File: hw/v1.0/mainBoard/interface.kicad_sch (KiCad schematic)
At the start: 30 parts, among them J1 MQ-7, J13 PM1003, J2 VEML7700, J3 SHT40, J5 ML8511, J7 BMP388, J8 PMS5003, Q16 2N7002, Q17 2N7002, Q3 AO3401A, Q4 2N7002, Q5 AO3401A, Q6 2N7002, Q7 AO3401A, Q8 2N7002

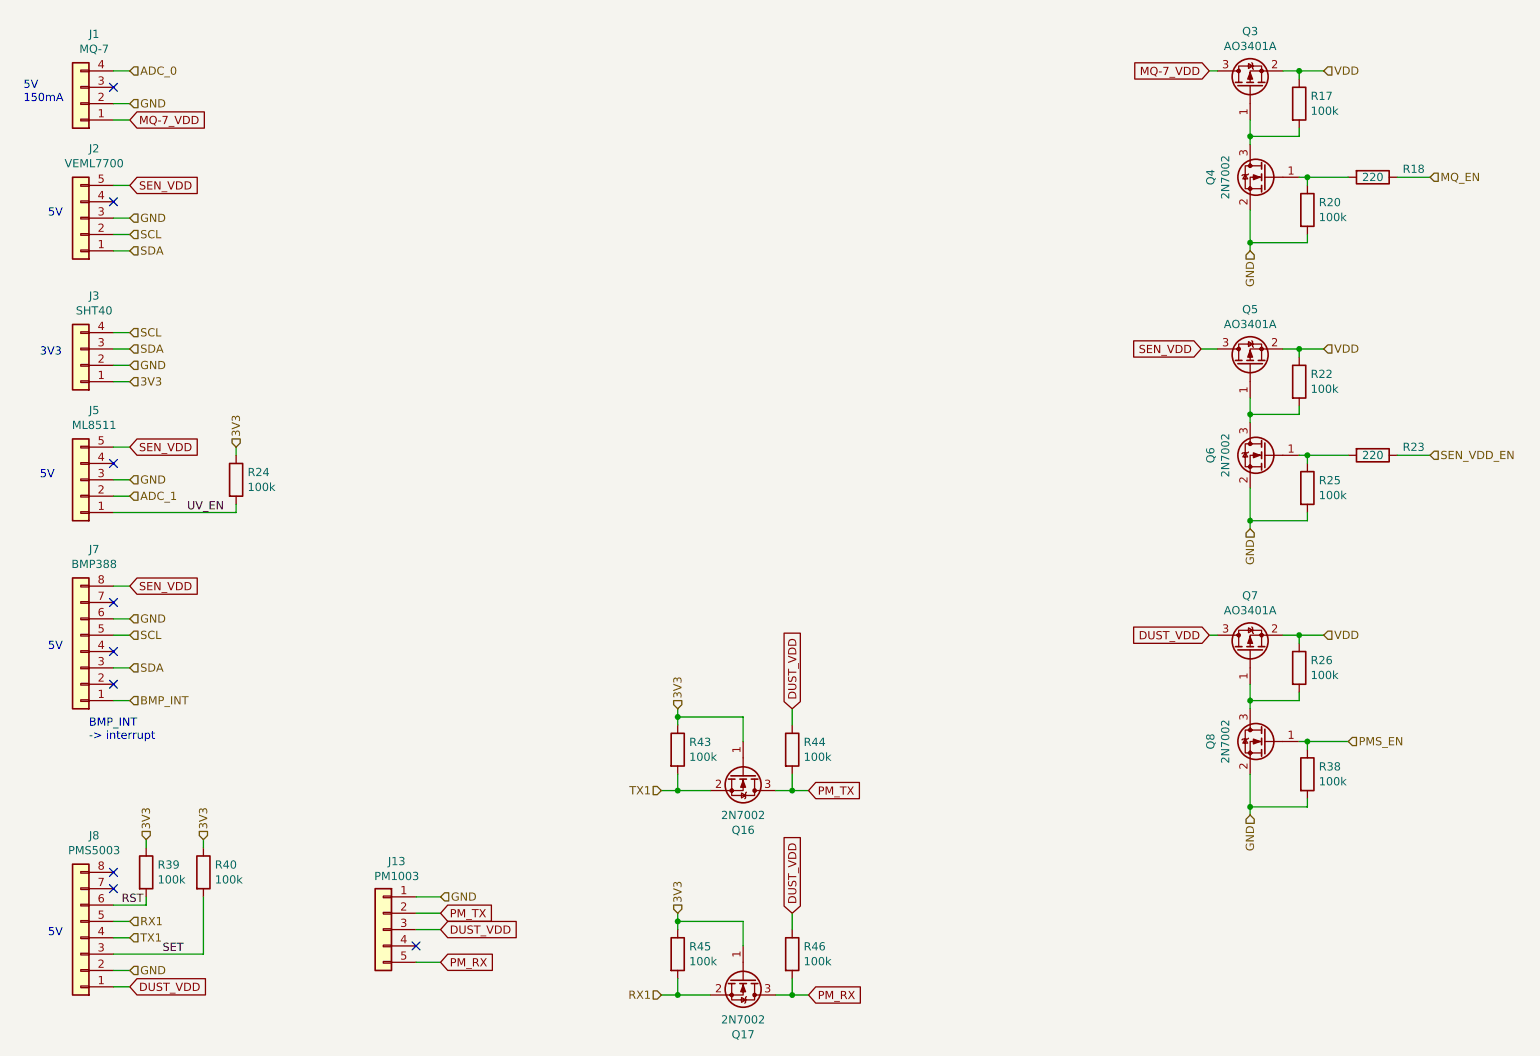
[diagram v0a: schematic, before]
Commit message: Start routing PCB
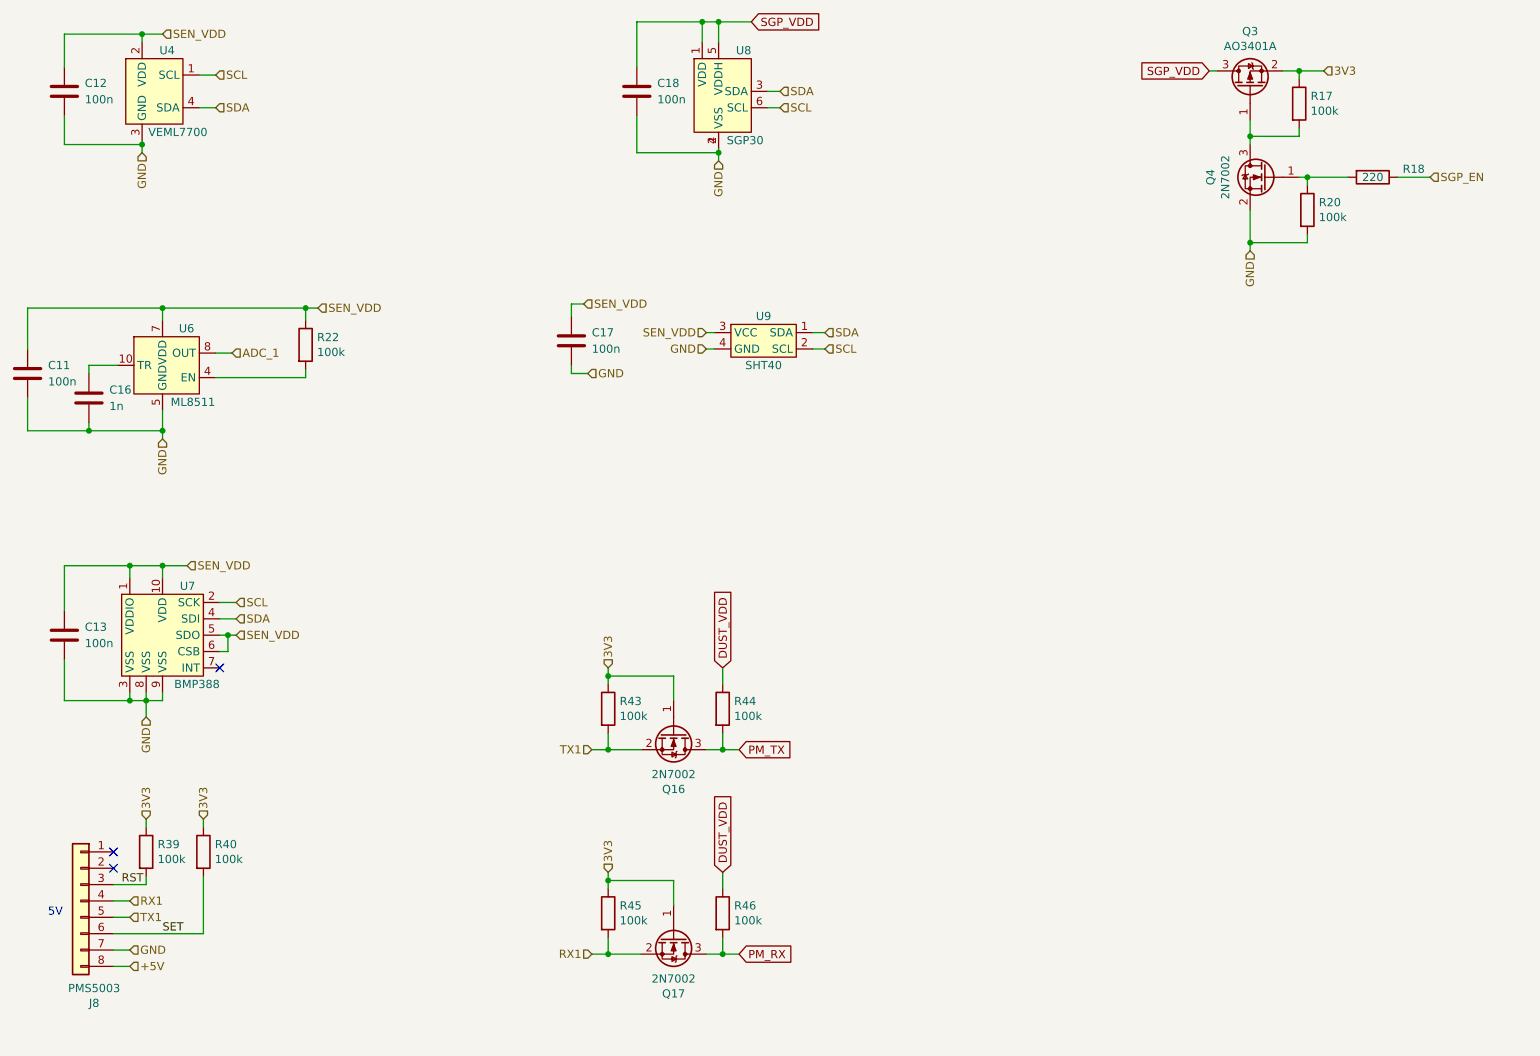
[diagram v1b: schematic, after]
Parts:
- removed J1: MQ-7, Connector_PinSocket_2.54mm:PinSocket_1x04_P2.54mm_Vertical, symbol Connector_Generic:Conn_01x04
- removed J13: PM1003, Connector_PinHeader_2.54mm:PinHeader_1x05_P2.54mm_Vertical, symbol Connector_Generic:Conn_01x05
- removed J2: VEML7700, Connector_PinSocket_2.54mm:PinSocket_1x05_P2.54mm_Vertical, symbol Connector_Generic:Conn_01x05
- removed J3: SHT40, Connector_PinSocket_2.54mm:PinSocket_1x04_P2.54mm_Vertical, symbol Connector_Generic:Conn_01x04
- removed J5: ML8511, Connector_PinSocket_2.54mm:PinSocket_1x05_P2.54mm_Vertical, symbol Connector_Generic:Conn_01x05
- removed J7: BMP388, Connector_PinSocket_2.54mm:PinSocket_1x08_P2.54mm_Vertical, symbol Connector_Generic:Conn_01x08
- removed Q5, Q7: AO3401A, Package_TO_SOT_SMD:SOT-23, symbol Device:Q_PMOS_GSD
- removed Q6, Q8: 2N7002, Package_TO_SOT_SMD:SOT-23, symbol Transistor_FET:2N7002
- removed R23: 220, Resistor_SMD:R_0402_1005Metric, symbol Device:R
- removed R24, R25, R26, R38: 100k, Resistor_SMD:R_0402_1005Metric, symbol Device:R
- added C11, C12, C13, C17, C18: 100n, Capacitor_SMD:C_0603_1608Metric, symbol Device:C
- added C16: 1n, Capacitor_SMD:C_0805_2012Metric, symbol Device:C
- added U4: VEML7700, mainBoard:VEML7700, symbol mainBoard:VEML7700
- added U6: ML8511, mainBoard:ML8511, symbol mainBoard:ML8511
- added U7: BMP388, mainBoard:BMP388, symbol mainBoard:BMP388
- added U8: SGP30, mainBoard:SGP30, symbol mainBoard:SGP30
- added U9: SHT40, mainBoard:SHT40, symbol mainBoard:SHT40
- R17, R18, R20, R22, R39, R40, R43, R44, R45, R46: footprint Resistor_SMD:R_0402_1005Metric -> Resistor_SMD:R_0805_2012Metric
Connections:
- net 3V3: now also Q3.2 (S), R17.1
- net ADC_1: now also U6.8 (OUT)
- net DUST_VDD: no longer J8.1 (Pin_1)
- net GND: now also J8.7 (Pin_7), C11.2, C12.2, C13.2, C16.2, C17.2, C18.2, U4.3 (GND), U6.5 (GND), U7.3 (VSS), U7.8 (VSS), U7.9 (VSS), U8.2 (VSS), U8.4, U9.4 (GND); no longer J8.2 (Pin_2)
- net RST: now also J8.3 (Pin_3); no longer J8.6 (Pin_6)
- net RX1: now also J8.4 (Pin_4); no longer J8.5 (Pin_5)
- net SCL: now also U4.1 (SCL), U7.2 (SCK), U8.6 (SCL), U9.2 (SCL)
- net SDA: now also U4.4 (SDA), U7.4 (SDI), U8.3 (SDA), U9.1 (SDA)
- net SEN_VDD: now also R22.1, C11.1, C12.1, C13.1, C17.1, U4.2 (VDD), U6.7 (VDD), U7.1 (VDDIO), U7.10 (VDD), U7.5 (SDO), U7.6 (CSB), U9.3 (VCC)
- net SET: now also J8.6 (Pin_6); no longer J8.3 (Pin_3)
- net TX1: now also J8.5 (Pin_5); no longer J8.4 (Pin_4)
- net +5V: now reaches J8.8 (Pin_8)
- net at R22.2: now also U6.4 (EN)
- net MQ-7_VDD renamed SGP_VDD
- net SGP_VDD: now also C18.1, U8.1 (VDD), U8.5 (VDDH)
- net MQ_EN renamed SGP_EN
- removed net VDD: Q3.2 (S), R17.1, R22.1
- new net: C16.1, U6.10 (TR)
- no-connect marks 9 -> 3
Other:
- note removed: "3V3"
- note removed: "5V 150mA"
- note removed: "BMP_INT -> interrupt"
- moved on the sheet: J8, Q16, Q17, R39, R40, R43, R44, R45, R46

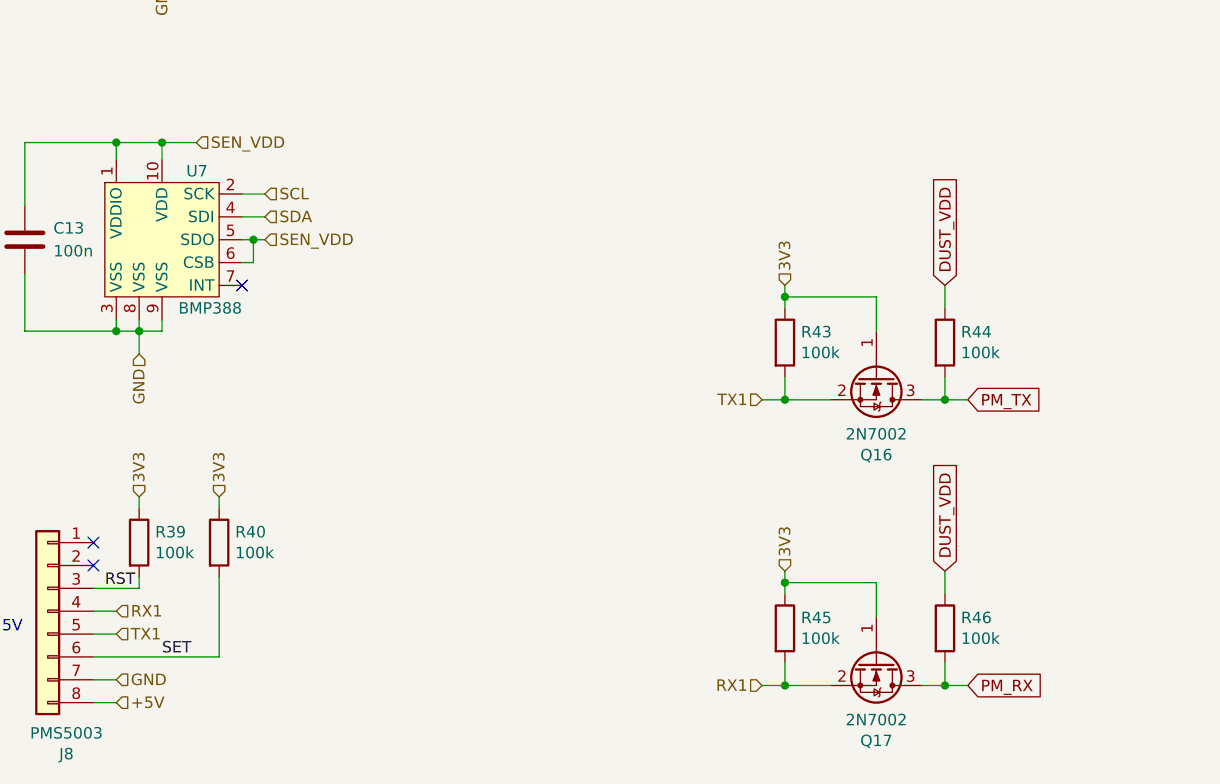
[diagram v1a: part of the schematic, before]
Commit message: More component placement in mainboard
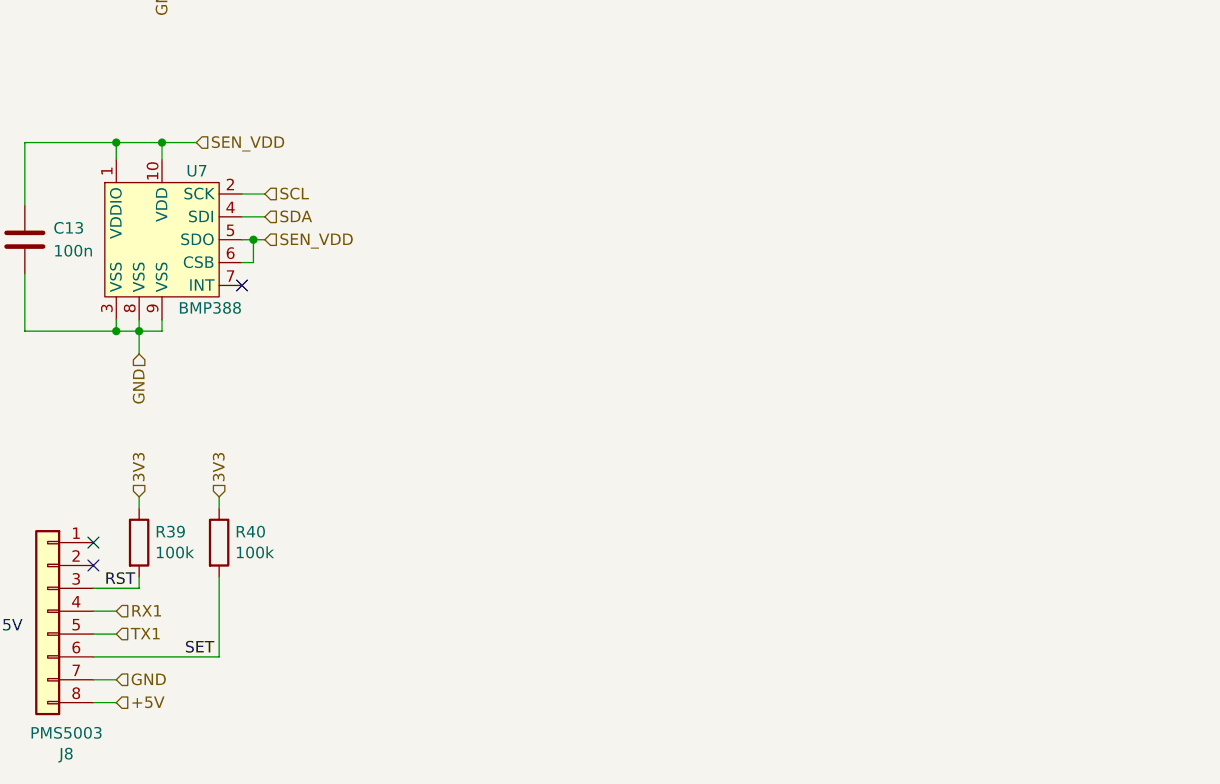
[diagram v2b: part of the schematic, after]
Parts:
- removed Q16, Q17: 2N7002, Package_TO_SOT_SMD:SOT-23, symbol Transistor_FET:2N7002
- removed R43, R44, R45, R46: 100k, Resistor_SMD:R_0805_2012Metric, symbol Device:R

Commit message: Maybe final component placement
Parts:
- added C22, C23: 1u, Capacitor_SMD:C_0805_2012Metric, symbol Device:C
- added Q7, Q8: 2N7002, Package_TO_SOT_SMD:SOT-23, symbol Transistor_FET:2N7002
- added R25, R26, R27, R28: 100k, Resistor_SMD:R_0805_2012Metric, symbol Device:R
- added U11: NCP115ASN180T2G, Package_SO:TSOP-5_1.65x3.05mm_P0.95mm, symbol mainBoard:NCP115ASN180T2G
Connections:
- net 3V3: now also R27.1, R28.1
- net GND: now also C22.2, C23.2, U11.2 (GND)
- net SCL: now also Q8.3 (D), R28.2; no longer U8.6 (SCL)
- net SDA: now also Q7.3 (D), R27.2; no longer U8.3 (SDA)
- net SGP_VDD: now also C22.1, Q7.1 (G), Q8.1 (G), R25.1, R26.1, U11.5 (OUT); no longer Q3.3 (D)
- new net: C23.1, Q3.3 (D), U11.1 (IN), U11.3 (EN)
- new net SCL_1V8: Q8.2 (S), R26.2, U8.6 (SCL)
- new net SDA_1V8: Q7.2 (S), R25.2, U8.3 (SDA)
